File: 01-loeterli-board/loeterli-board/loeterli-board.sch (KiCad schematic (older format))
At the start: 26 parts, among them J1 AC_IN_P, J2 AC_IN_N, J3 EARTH_IN, Q1 Q_NMOS_DSG, Q2 Q_NMOS_DSG, U1 VOM1271T

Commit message: new ac rect arch
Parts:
- removed C?: C, symbol Device:C
- removed J1: AC_IN_P, Connector_Wire:SolderWirePad_1x01_Drill2.5mm, symbol Connector_Generic:Conn_01x01
- removed J2: AC_IN_N, Connector_Wire:SolderWirePad_1x01_Drill2.5mm, symbol Connector_Generic:Conn_01x01
- removed J3: EARTH_IN, Connector_Wire:SolderWirePad_1x01_Drill2.5mm, symbol Connector_Generic:Conn_01x01
- removed J?: AC_OUT_P, Connector_Wire:SolderWirePad_1x01_Drill2.5mm, symbol Connector_Generic:Conn_01x01
- removed J?: AC_OUT_N, Connector_Wire:SolderWirePad_1x01_Drill2.5mm, symbol Connector_Generic:Conn_01x01
- removed J?: LV_P, Connector_Wire:SolderWirePad_1x01_Drill2.5mm, symbol Connector_Generic:Conn_01x01
- removed J?: LV_N, Connector_Wire:SolderWirePad_1x01_Drill2.5mm, symbol Connector_Generic:Conn_01x01
- removed PS?: IRM-02-9, Converter_ACDC:Converter_ACDC_MeanWell_IRM-02-xx_THT, symbol Converter_ACDC:IRM-02-9
- removed Q1, Q2: Q_NMOS_DSG, symbol Device:Q_NMOS_DSG
- removed U?: NCP1117-3.3_TO252, Package_TO_SOT_SMD:TO-252-2, symbol Regulator_Linear:NCP1117-3.3_TO252
- added C10, C8, C9: C, Capacitor_SMD:C_0603_1608Metric, symbol Device:C
- added C11, C12, C13: C, Capacitor_SMD:C_1206_3216Metric, symbol Device:C
- added C14, C15, C3: CP1, Capacitor_THT:CP_Radial_D10.0mm_P5.00mm_P7.50mm, symbol Device:CP1
- added D1, D2: D, Diode_SMD:D_0603_1608Metric, symbol Device:D
- added D3, D4, D5, D6, D7: FSV12100V, Package_TO_SOT_SMD:TO-277A, symbol Diode:VS-6ESU06
- added H1, H2, H3, H4: MountingHole_Pad, MountingHole:MountingHole_3.2mm_M3_Pad_Via, symbol Mechanical:MountingHole_Pad
- added J4: DIN-6, symbol Connector:DIN-6
- added J5: Screw_Terminal_01x03, TerminalBlock_Phoenix:TerminalBlock_Phoenix_MKDS-1,5-3-5.08_1x03_P5.08mm_Horizontal, symbol Connector:Screw_Terminal_01x03
- added Q1: PSMN5R2-60YL, Package_TO_SOT_SMD:LFPAK56, symbol Transistor_FET:PSMN5R2-60YL
- added R3: 10k, Resistor_SMD:R_1206_3216Metric, symbol Device:R
- added R4, R5, R6: R, Resistor_SMD:R_0603_1608Metric, symbol Device:R
- added SW2, SW3, SW4: SW_Push, Button_Switch_THT:SW_PUSH_6mm_H4.3mm, symbol Switch:SW_Push
- added U3: R-78HB3.3-0.5, Converter_DCDC:Converter_DCDC_RECOM_R-78HB-0.5_THT, symbol Regulator_Switching:R-78HB3.3-0.5
- added U4: TSZ121, Package_TO_SOT_SMD:SOT-23-5, symbol loeterli:TSZ121
- added U?: AD8223, symbol Amplifier_Instrumentation:AD620
- C1, C2: renamed from C?; footprint (none) -> Capacitor_SMD:C_1206_3216Metric
- C4, C5, C6, C7: renamed from C?; footprint (none) -> Capacitor_SMD:C_0603_1608Metric
- F1: footprint (none) -> Fuse:Fuseholder_Cylinder-5x20mm_Schurter_0031_8201_Horizontal_Open
- J8: renamed from J?; footprint (none) -> Connector_Wire:SolderWirePad_1x03_P4.445mm_Drill1.5mm
- R1: footprint (none) -> Resistor_SMD:R_1206_3216Metric
- R2: renamed from R?; footprint (none) -> Resistor_SMD:R_0603_1608Metric
- SW1: renamed from SW?; footprint (none) -> Button_Switch_THT:SW_PUSH_6mm_H4.3mm
- U1: footprint (none) -> Package_SO:SOP-4_3.8x4.1mm_P2.54mm
- gave numbers to parts that had none: 2
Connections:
- net labels added: Earth, TEMP, V_RECT
- net labels removed: +5V, LV_N, LV_P
- wire segments 74 -> 119
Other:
- note added: "Heater"
- note added: "INVERTING?\nINSTRUMENTATION"
- note added: "Thermocouple"
- moved on the sheet: C2, F1, R1, U1, U5

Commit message: added readme image + misc
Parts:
- removed J4: DIN-6, symbol Connector:DIN-6
- removed J8: Conn_01x03, Connector_Wire:SolderWirePad_1x03_P4.445mm_Drill1.5mm, symbol Connector_Generic:Conn_01x03
- added D8, D9: LED, LED_THT:LED_D4.0mm, symbol Device:LED
- added J1: RPC1-12RB-6P, loeterli:RPC1-12RB-6P, symbol loeterli:RPC1-12RB-6P
- gave numbers to parts that had none: 1
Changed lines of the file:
@@
-	1    0    0    -1
-$EndComp
-$Comp
-L Connector_Generic:Conn_01x03 J8
-U 1 1 5ECBCD4A
-P 10250 2400
-F 0 "J8" H 10330 2442 50  0000 L CNN
-F 1 "Conn_01x03" H 10330 2351 50  0000 L CNN
-F 2 "Connector_Wire:SolderWirePad_1x03_P4.445mm_Drill1.5mm" H 10250 2400 50  0001 C CNN
-F 3 "~" H 10250 2400 50  0001 C CNN
-	1    10250 2400
 	1    0    0    -1
 $EndComp
@@
 Connection ~ 6400 1250
 $Comp
-L Connector:DIN-6 J4
-U 1 1 5EE68664
-P 10450 1650
-F 0 "J4" H 10450 2131 50  0000 C CNN
-F 1 "DIN-6" H 10450 2040 50  0000 C CNN
-F 2 "" H 10450 1650 50  0001 C CNN
-F 3 "http://www.mouser.com/ds/2/18/40_c091_abd_e-75918.pdf" H 10450 1650 50  0001 C CNN
-	1    10450 1650
-	1    0    0    -1
-$EndComp
-$Comp
 L Connector:Screw_Terminal_01x03 J5
 U 1 1 5EE6CFB7
@@
 $EndComp
 $Comp
-L Amplifier_Instrumentation:AD620 U?
+L Amplifier_Instrumentation:AD620 U6
 U 1 1 5EE96E22
 P 7900 2800
-F 0 "U?" H 8344 2846 50  0000 L CNN
+F 0 "U6" H 8344 2846 50  0000 L CNN
 F 1 "AD8223" H 8344 2755 50  0000 L CNN
 F 2 "" H 7900 2800 50  0001 C CNN
@@
 	1    0    0    -1
 $EndComp
+$Comp
+L loeterli:RPC1-12RB-6P J1
+U 1 1 5ECA846E
+P 10550 1650
+F 0 "J1" H 10550 2131 50  0000 C CNN
+F 1 "RPC1-12RB-6P" H 10550 2040 50  0000 C CNN
+F 2 "loeterli:RPC1-12RB-6P" H 10700 2000 50  0001 C CNN
+F 3 "" H 10700 2000 50  0001 C CNN
+	1    10550 1650
+	1    0    0    -1
+$EndComp
+$Comp
+L Device:LED D8
+U 1 1 5ECBD91D
+P 1400 5950
+F 0 "D8" H 1393 6167 50  0000 C CNN
+F 1 "LED" H 1393 6076 50  0000 C CNN
+F 2 "LED_THT:LED_D4.0mm" H 1400 5950 50  0001 C CNN
+F 3 "~" H 1400 5950 50  0001 C CNN
+	1    1400 5950
+	1    0    0    -1
+$EndComp
+$Comp
+L Device:LED D9
+U 1 1 5ECBEB59
+P 1400 6250
+F 0 "D9" H 1393 6467 50  0000 C CNN
+F 1 "LED" H 1393 6376 50  0000 C CNN
+F 2 "LED_THT:LED_D4.0mm" H 1400 6250 50  0001 C CNN
+F 3 "~" H 1400 6250 50  0001 C CNN
+	1    1400 6250
+	1    0    0    -1
+$EndComp

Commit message: misc
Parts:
- added D10: D, Diode_SMD:D_0603_1608Metric, symbol Device:D
- added R7: 100k, Resistor_SMD:R_1206_3216Metric, symbol Device:R
- U6: value AD8223 -> AD8227
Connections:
- net labels added: H+, ZCD
- wire segments 119 -> 122
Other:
- note added: "EARTH"
- note added: "GND"
- note added: "H+"
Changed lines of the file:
@@
 	850  1150 900  1150
 Wire Wire Line
-	9350 2300 10050 2300
+	9350 2300 9550 2300
 $Comp
 L Device:R R1
@@
 $EndComp
 Wire Notes Line
-	10400 2300 10500 2300
-Wire Notes Line
-	10500 2300 10500 2100
-Wire Notes Line
-	10500 2100 10700 2100
-Wire Notes Line
-	10700 2100 10700 2150
-Wire Notes Line
-	10650 2150 10650 2300
-Wire Notes Line
-	10650 2300 10750 2300
-Wire Notes Line
-	10750 2300 10750 2150
-Wire Notes Line
-	10650 2150 10750 2150
-Wire Notes Line
-	10700 2300 10700 2400
-Wire Notes Line
-	10850 2550 10500 2550
-Wire Notes Line
-	10500 2550 10500 2500
-Wire Notes Line
-	10500 2500 10400 2500
-Wire Notes Line
-	10400 2400 10850 2400
-Wire Notes Line
-	10850 2400 10850 2550
-Wire Notes Line
-	10850 2500 10900 2500
-Wire Notes Line
-	10900 2500 10900 2450
-Wire Notes Line
-	10900 2450 10850 2450
+	10200 2400 10300 2400
+Wire Notes Line
+	10300 2400 10300 2200
+Wire Notes Line
+	10300 2200 10500 2200
+Wire Notes Line
+	10500 2200 10500 2250
+Wire Notes Line
+	10450 2250 10450 2400
+Wire Notes Line
+	10450 2400 10550 2400
+Wire Notes Line
+	10550 2400 10550 2250
+Wire Notes Line
+	10450 2250 10550 2250
+Wire Notes Line
+	10500 2400 10500 2500
+Wire Notes Line
+	10650 2650 10300 2650
+Wire Notes Line
+	10300 2650 10300 2600
+Wire Notes Line
+	10300 2600 10200 2600
+Wire Notes Line
+	10200 2500 10650 2500
+Wire Notes Line
+	10650 2500 10650 2650
+Wire Notes Line
+	10650 2600 10700 2600
+Wire Notes Line
+	10700 2600 10700 2550
+Wire Notes Line
+	10700 2550 10650 2550
 $Comp
 L power:GND #PWR0105
 U 1 1 5ECD52F9
-P 9700 2500
-F 0 "#PWR0105" H 9700 2250 50  0001 C CNN
-F 1 "GND" H 9705 2327 50  0000 C CNN
-F 2 "" H 9700 2500 50  0001 C CNN
-F 3 "" H 9700 2500 50  0001 C CNN
-	1    9700 2500
-	1    0    0    -1
-$EndComp
-Wire Wire Line
-	10050 2500 10000 2500
-Wire Wire Line
-	10000 2500 10000 2550
+P 10200 1850
+F 0 "#PWR0105" H 10200 1600 50  0001 C CNN
+F 1 "GND" H 10205 1677 50  0000 C CNN
+F 2 "" H 10200 1850 50  0001 C CNN
+F 3 "" H 10200 1850 50  0001 C CNN
+	1    10200 1850
+	1    0    0    -1
+$EndComp
+Wire Wire Line
+	10250 1550 10200 1550
+Wire Wire Line
+	10200 1550 10200 1600
 Connection ~ 6400 950
 Wire Wire Line
@@
 Wire Wire Line
 	9150 3700 9600 3700
-Text Notes 10650 2650 0    50   ~ 0
+Text Notes 10450 2750 0    50   ~ 0
 Thermocouple
-Text Notes 10800 2300 0    50   ~ 0
+Text Notes 10600 2400 0    50   ~ 0
 Heater
 $Comp
@@
 L power:Earth #PWR0118
 U 1 1 5ED9F120
-P 10000 2550
-F 0 "#PWR0118" H 10000 2300 50  0001 C CNN
-F 1 "Earth" H 10000 2400 50  0001 C CNN
-F 2 "" H 10000 2550 50  0001 C CNN
-F 3 "~" H 10000 2550 50  0001 C CNN
-	1    10000 2550
-	1    0    0    -1
-$EndComp
-Wire Wire Line
-	10050 2400 9700 2400
-Wire Wire Line
-	9700 2400 9700 2500
+P 10200 1600
+F 0 "#PWR0118" H 10200 1350 50  0001 C CNN
+F 1 "Earth" H 10200 1450 50  0001 C CNN
+F 2 "" H 10200 1600 50  0001 C CNN
+F 3 "~" H 10200 1600 50  0001 C CNN
+	1    10200 1600
+	1    0    0    -1
+$EndComp
+Wire Wire Line
+	10250 1750 10200 1750
+Wire Wire Line
+	10200 1750 10200 1850
 $Comp
 L power:GND #PWR0119
@@
 P 7900 2800
 F 0 "U6" H 8344 2846 50  0000 L CNN
-F 1 "AD8223" H 8344 2755 50  0000 L CNN
+F 1 "AD8227" H 8344 2755 50  0000 L CNN
 F 2 "" H 7900 2800 50  0001 C CNN
 F 3 "" H 7900 2800 50  0001 C CNN
@@
 	1    0    0    -1
 $EndComp
+Text Notes 9950 2650 0    50   ~ 0
+EARTH
+Text Notes 9950 2550 0    50   ~ 0
+GND
+Text Notes 9950 2450 0    50   ~ 0
+H+
+Text GLabel 9550 2300 2    50   Output ~ 0
+H+
+Text GLabel 10850 1550 2    50   Input ~ 0
+H+
+$Comp
+L Device:R R7
+U 1 1 5ECD2BEA
+P 3900 2100
+F 0 "R7" H 3970 2146 50  0000 L CNN
+F 1 "100k" H 3970 2055 50  0000 L CNN
+F 2 "Resistor_SMD:R_1206_3216Metric" V 3830 2100 50  0001 C CNN
+F 3 "~" H 3900 2100 50  0001 C CNN
+	1    3900 2100
+	0    -1   -1   0
+$EndComp
+$Comp
+L Device:D D10
+U 1 1 5ECD73F5
+P 4200 1950
+F 0 "D10" V 4154 2030 50  0000 L CNN
+F 1 "D" V 4245 2030 50  0000 L CNN
+F 2 "Diode_SMD:D_0603_1608Metric" H 4200 1950 50  0001 C CNN
+F 3 "~" H 4200 1950 50  0001 C CNN
+	1    4200 1950
+	0    1    1    0
+$EndComp
+$Comp
+L power:+3.3V #PWR0104
+U 1 1 5ECDB90F
+P 4200 1750
+F 0 "#PWR0104" H 4200 1600 50  0001 C CNN
+F 1 "+3.3V" H 4215 1923 50  0000 C CNN
+F 2 "" H 4200 1750 50  0001 C CNN
+F 3 "" H 4200 1750 50  0001 C CNN
+	1    4200 1750
+	1    0    0    -1
+$EndComp
+Wire Wire Line
+	4200 1800 4200 1750
+Wire Wire Line
+	4050 2100 4200 2100
+Wire Wire Line
+	4200 2100 4550 2100
+Connection ~ 4200 2100
+Text GLabel 4550 2100 2    50   Output ~ 0
+ZCD
+Text GLabel 3750 2100 0    50   Input ~ 0
+V_RECT
 $EndSCHEMATC

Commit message: thermocouple circuit instr and sim
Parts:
- removed R4, R5: R, Resistor_SMD:R_0603_1608Metric, symbol Device:R
- removed U4: TSZ121, Package_TO_SOT_SMD:SOT-23-5, symbol loeterli:TSZ121
- added R?: 845, symbol Device:R
- added R? (x2): 1k, symbol Device:R
- R3: value 10k -> 100
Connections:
- wire segments 122 -> 130
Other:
- note removed: "INVERTING?\nINSTRUMENTATION"
- moved on the sheet: C10, C8, C9, D1, D2, R3, R6, U6

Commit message: changed tc amp
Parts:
- removed D1, D2: D, Diode_SMD:D_0603_1608Metric, symbol Device:D
- added C16: C, Capacitor_SMD:C_0603_1608Metric, symbol Device:C
- added F2: Fuse, Fuse:Fuse_1206_3216Metric, symbol Device:Fuse
- added J3: Conn_01x04, Connector_PinHeader_2.54mm:PinHeader_1x04_P2.54mm_Vertical, symbol Connector_Generic:Conn_01x04
- added R12: 100, Resistor_SMD:R_0603_1608Metric, symbol Device:R
- added R4, R8, R9: 100k, Resistor_SMD:R_1206_3216Metric, symbol Device:R
- D3, D4, D5, D6, D7: symbol Diode:VS-6ESU06 -> loeterli-board-rescue:VS-6ESU06-Diode
- R10, R11, R5: renamed from R?; footprint (none) -> Resistor_SMD:R_0603_1608Metric
- R3: footprint Resistor_SMD:R_1206_3216Metric -> Resistor_SMD:R_0603_1608Metric
- U6: footprint (none) -> Package_SO:MSOP-8_3x3mm_P0.65mm
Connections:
- net labels added: H-, TC_EARTH
- wire segments 130 -> 133
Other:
- moved on the sheet: Q1, R1, R10, R11, U1, U5

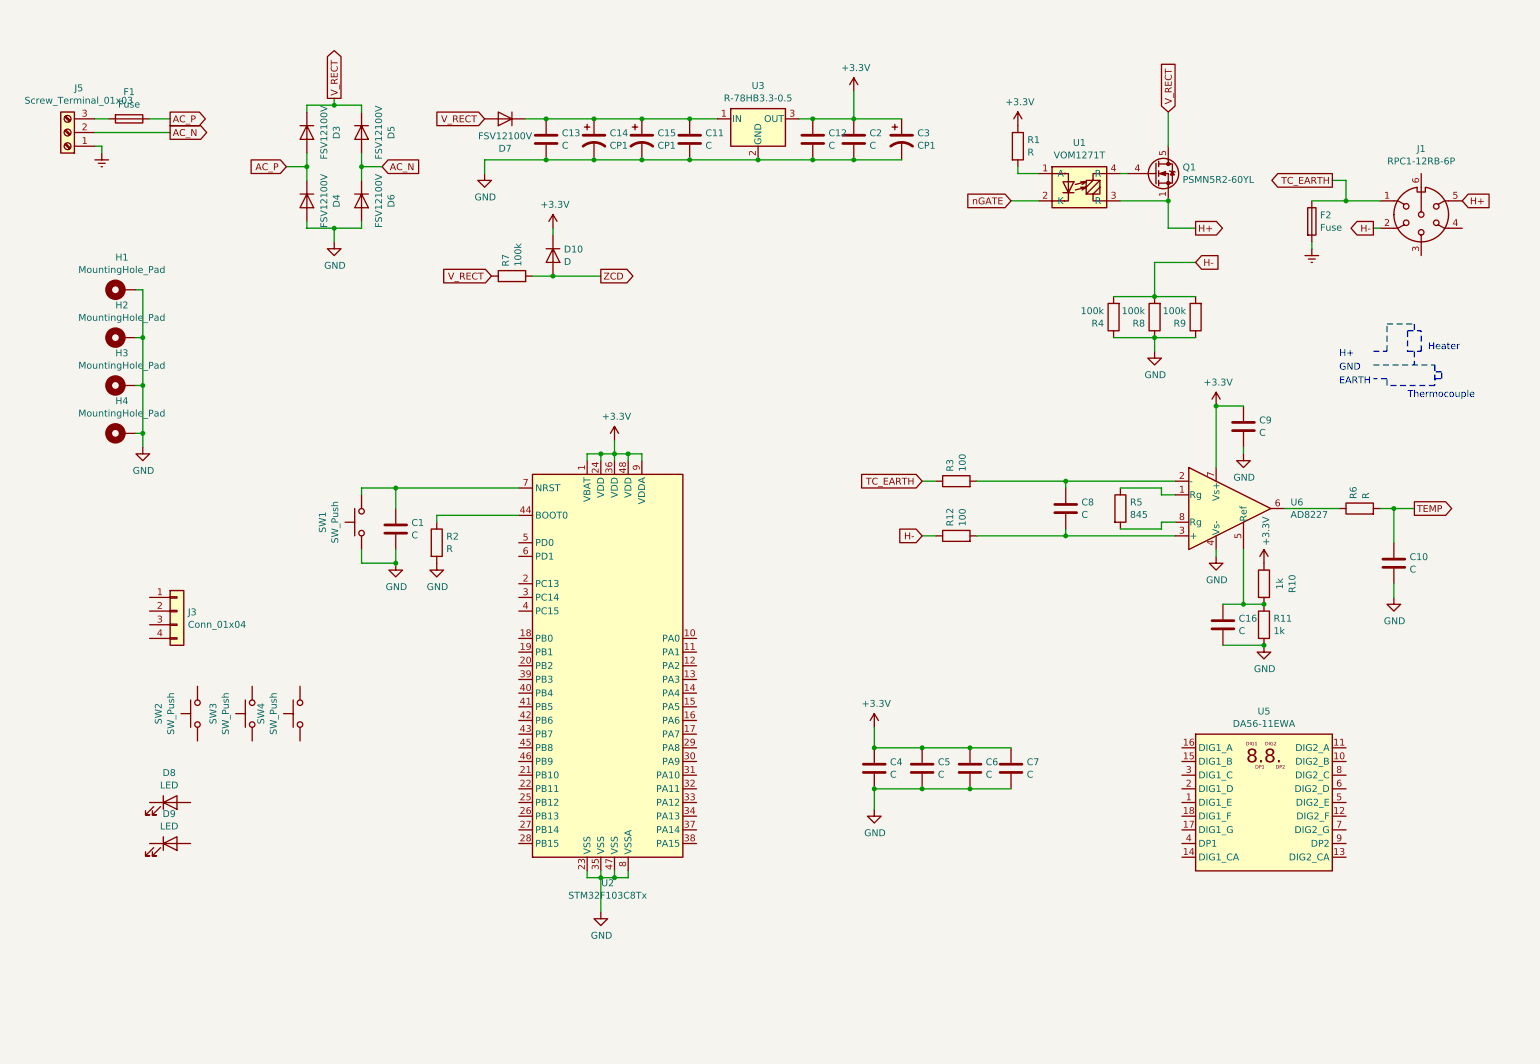
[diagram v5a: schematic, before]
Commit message: logo + res for leds
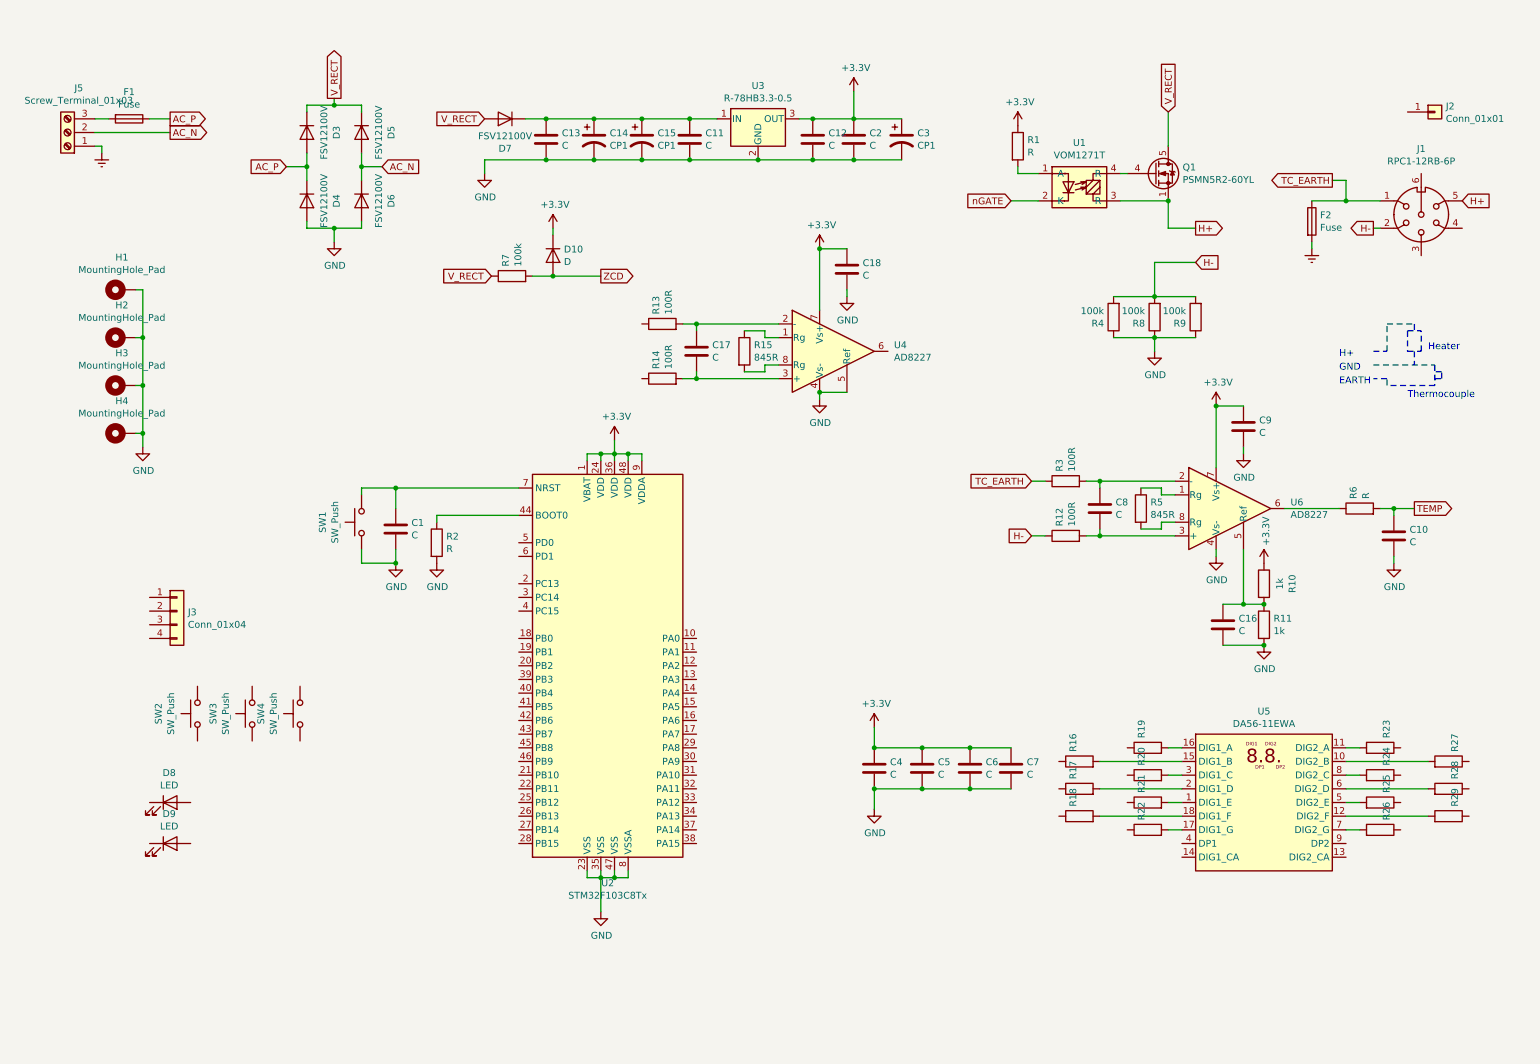
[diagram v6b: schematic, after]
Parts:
- added C17, C18: C, Capacitor_SMD:C_0603_1608Metric, symbol Device:C
- added J2: Conn_01x01, loeterli:handpiece-holder, symbol Connector_Generic:Conn_01x01
- added R13, R14: 100R, Resistor_SMD:R_0603_1608Metric, symbol Device:R
- added R15: 845R, Resistor_SMD:R_0603_1608Metric, symbol Device:R
- added R16, R17, R18, R19, R20, R21, R22, R23, R24, R25, R26, R27, R28, R29: 680R, Resistor_SMD:R_0603_1608Metric, symbol Device:R
- added U4: AD8227, Package_SO:MSOP-8_3x3mm_P0.65mm, symbol Amplifier_Instrumentation:AD620
- R12, R3: value 100 -> 100R
- R5: value 845 -> 845R
- SW2, SW3, SW4: footprint Button_Switch_THT:SW_PUSH_6mm_H4.3mm -> Button_Switch_THT:SW_PUSH_6mm_H7.3mm
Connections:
- net +3V3: now also C18.1, U4.7 (Vs+)
- net GND: now also C18.2, U4.4 (Vs-), U4.5 (Ref)
- net at U5.1 (DIG1_E): now also R21.2
- net at U5.10 (DIG2_B): now also R27.2
- net at U5.11 (DIG2_A): now also R23.2
- net at U5.12 (DIG2_F): now also R29.2
- net at U5.15 (DIG1_B): now also R16.2
- net at U5.16 (DIG1_A): now also R19.2
- net at U5.17 (DIG1_G): now also R22.2
- net at U5.18 (DIG1_F): now also R18.2
- net at U5.2 (DIG1_D): now also R17.2
- net at U5.3 (DIG1_C): now also R20.2
- net at U5.5 (DIG2_E): now also R25.2
- net at U5.6 (DIG2_D): now also R28.2
- net at U5.7 (DIG2_G): now also R26.2
- net at U5.8 (DIG2_C): now also R24.2
- new net: R15.1, U4.1 (Rg)
- new net: C17.1, R13.2, U4.2 (-)
- new net: C17.2, R14.2, U4.3 (+)
- new net: R15.2, U4.8 (Rg)
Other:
- moved on the sheet: C10, C8, R12, R3, R5
